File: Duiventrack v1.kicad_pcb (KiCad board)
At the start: 2 copper layers, 22.6 x 12.8 mm, 30 parts, among them P1 CONN_01X07, P2 CONN_01X02, U1 MCP1711-SOT23-5, U2 SP-ABZ-G

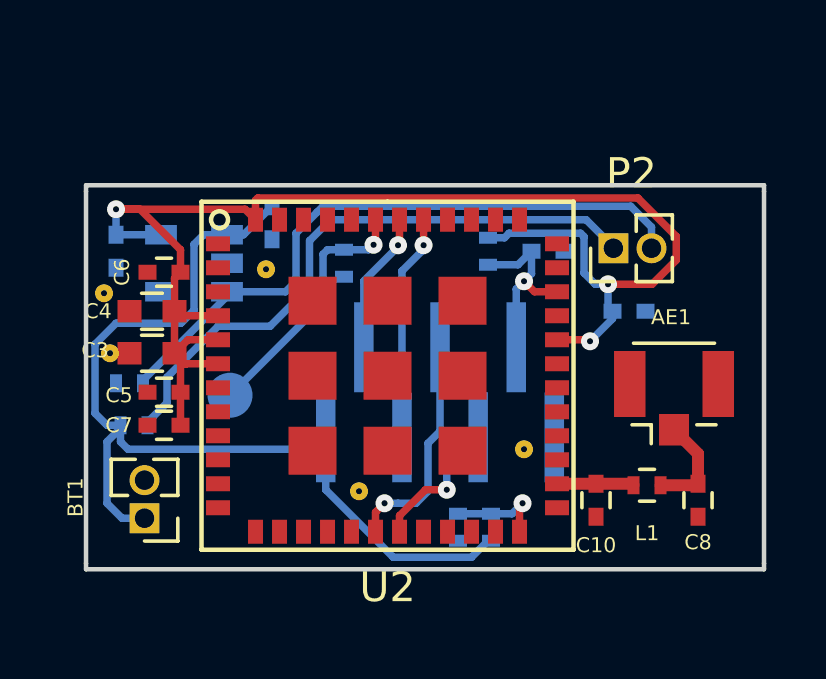
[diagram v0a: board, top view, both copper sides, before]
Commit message: Ground vias toegevoegd
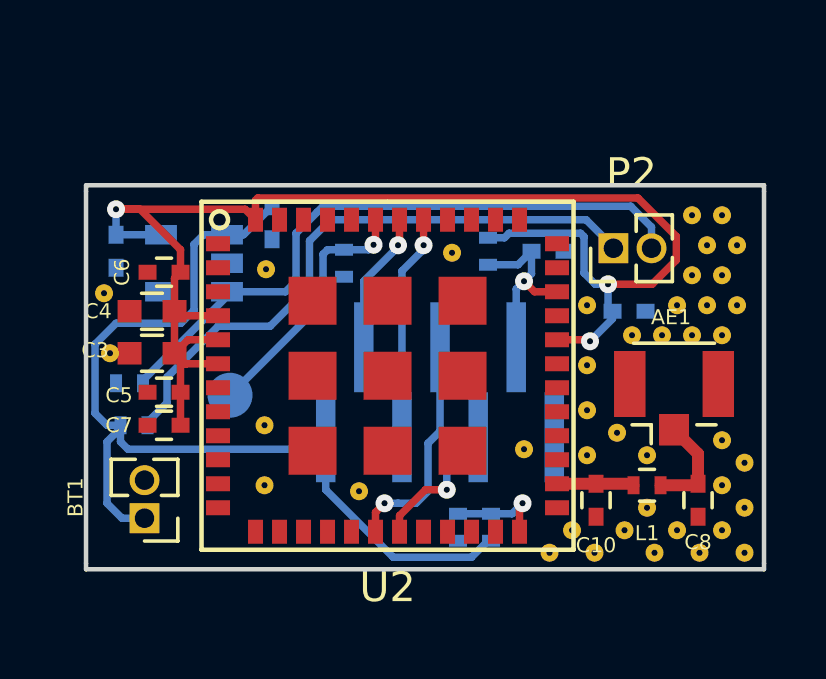
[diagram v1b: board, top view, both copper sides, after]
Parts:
- added REF**: Via 0,6 0,2, Footprint:Via0,6, F.Cu at (145.8, 95.0)
- added REF**: Via 0,6 0,2, Footprint:Via0,6, F.Cu at (158.8, 97.2)
- added REF**: Via 0,6 0,2, Footprint:Via0,6, F.Cu at (158.5, 95.8)
- added REF**: Via 0,6 0,2, Footprint:Via0,6, F.Cu at (159.5, 96.5)
- added REF**: Via 0,6 0,2, Footprint:Via0,6, F.Cu at (160.2, 97.2)
- added REF**: Via 0,6 0,2, Footprint:Via0,6, F.Cu at (161.8, 97.2)
- added REF**: Via 0,6 0,2, Footprint:Via0,6, F.Cu at (161.0, 96.5)
- added REF**: Via 0,6 0,2, Footprint:Via0,6, F.Cu at (161.8, 95.8)
- added REF**: Via 0,6 0,2, Footprint:Via0,6, F.Cu at (161.0, 95.0)
- added REF**: Via 0,6 0,2, Footprint:Via0,6, F.Cu at (156.5, 91.0)
- added REF**: Via 0,6 0,2, Footprint:Via0,6, F.Cu at (156.5, 92.5)
- added REF**: Via 0,6 0,2, Footprint:Via0,6, F.Cu at (145.8, 93.0)
- added REF**: Via 0,6 0,2, Footprint:Via0,6, F.Cu at (161.8, 94.2)
- added REF**: Via 0,6 0,2, Footprint:Via0,6, F.Cu at (160.0, 86.0)
- added REF**: Via 0,6 0,2, Footprint:Via0,6, F.Cu at (161.0, 86.0)
- added REF**: Via 0,6 0,2, Footprint:Via0,6, F.Cu at (161.5, 87.0)
- added REF**: Via 0,6 0,2, Footprint:Via0,6, F.Cu at (160.5, 87.0)
- added REF**: Via 0,6 0,2, Footprint:Via0,6, F.Cu at (160.0, 88.0)
- added REF**: Via 0,6 0,2, Footprint:Via0,6, F.Cu at (161.0, 88.0)
- added REF**: Via 0,6 0,2, Footprint:Via0,6, F.Cu at (161.5, 89.0)
- added REF**: Via 0,6 0,2, Footprint:Via0,6, F.Cu at (160.5, 89.0)
- added REF**: Via 0,6 0,2, Footprint:Via0,6, F.Cu at (159.5, 89.0)
- added REF**: Via 0,6 0,2, Footprint:Via0,6, F.Cu at (152.0, 87.2)
- added REF**: Via 0,6 0,2, Footprint:Via0,6, F.Cu at (161.0, 93.5)
- added REF**: Via 0,6 0,2, Footprint:Via0,6, F.Cu at (157.5, 93.2)
- added REF**: Via 0,6 0,2, Footprint:Via0,6, F.Cu at (156.5, 94.0)
- added REF**: Via 0,6 0,2, Footprint:Via0,6, F.Cu at (161.0, 90.0)
- added REF**: Via 0,6 0,2, Footprint:Via0,6, F.Cu at (160.0, 90.0)
- added REF**: Via 0,6 0,2, Footprint:Via0,6, F.Cu at (159.0, 90.0)
- added REF**: Via 0,6 0,2, Footprint:Via0,6, F.Cu at (156.5, 89.0)
- added REF**: Via 0,6 0,2, Footprint:Via0,6, F.Cu at (158.0, 90.0)
- added REF**: Via 0,6 0,2, Footprint:Via0,6, F.Cu at (158.5, 94.0)
- added REF**: Via 0,6 0,2, Footprint:Via0,6, F.Cu at (155.2, 97.2)
- added REF**: Via 0,6 0,2, Footprint:Via0,6, F.Cu at (156.0, 96.5)
- added REF**: Via 0,6 0,2, Footprint:Via0,6, F.Cu at (156.8, 97.2)
- added REF**: Via 0,6 0,2, Footprint:Via0,6, F.Cu at (157.8, 96.5)

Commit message: Crystal toegevoegd
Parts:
- removed the REF** at (145.8, 95.0)
- removed the REF** at (158.8, 97.2)
- removed the REF** at (158.5, 95.8)
- removed the REF** at (159.5, 96.5)
- removed the REF** at (160.2, 97.2)
- removed the REF** at (161.8, 97.2)
- removed the REF** at (161.0, 96.5)
- removed the REF** at (161.8, 95.8)
- removed the REF** at (161.0, 95.0)
- removed the REF** at (156.5, 92.5)
- removed the REF** at (145.8, 93.0)
- removed the REF** at (161.8, 94.2)
- removed the REF** at (160.0, 86.0)
- removed the REF** at (161.0, 86.0)
- removed the REF** at (161.5, 87.0)
- removed the REF** at (160.5, 87.0)
- removed the REF** at (160.0, 88.0)
- removed the REF** at (161.0, 88.0)
- removed the REF** at (161.5, 89.0)
- removed the REF** at (160.5, 89.0)
- removed the REF** at (159.5, 89.0)
- removed the REF** at (152.0, 87.2)
- removed the REF** at (161.0, 93.5)
- removed the REF** at (157.5, 93.2)
- removed the REF** at (161.0, 90.0)
- removed the REF** at (160.0, 90.0)
- removed the REF** at (159.0, 90.0)
- removed the REF** at (148.9, 95.2)
- removed the REF** at (145.8, 87.8)
- removed the REF** at (140.6, 90.6)
- removed the REF** at (154.4, 93.8)
- removed the REF** at (156.5, 89.0)
- removed the REF** at (140.4, 88.6)
- removed the REF** at (158.0, 90.0)
- removed the REF** at (158.5, 94.0)
- removed the REF** at (155.2, 97.2)
- removed the REF** at (156.0, 96.5)
- removed the REF** at (156.8, 97.2)
- removed the REF** at (157.8, 96.5)
- added C12: 20pF, Capacitors_SMD:C_0402, F.Cu at (151.5, 83.9)
- added C13: 20pF, Capacitors_SMD:C_0402, F.Cu at (143.5, 83.9)
- added REF**: Via 0,6 0,2, Footprint:Via0,6, F.Cu at (159.5, 86.0)
- added REF**: Via 0,6 0,2, Footprint:Via0,6, F.Cu at (157.5, 93.5)
- added REF**: Via 0,6 0,2, Footprint:Via0,6, F.Cu at (156.5, 93.0)
- added REF**: Via 0,6 0,2, Footprint:Via0,6, F.Cu at (156.5, 92.0)
- added REF**: Via 0,6 0,2, Footprint:Via0,6, F.Cu at (155.5, 97.0)
- added REF**: Via 0,6 0,2, Footprint:Via0,6, F.Cu at (156.5, 97.0)
- added REF**: Via 0,6 0,2, Footprint:Via0,6, F.Cu at (157.5, 97.0)
- added REF**: Via 0,6 0,2, Footprint:Via0,6, F.Cu at (158.0, 96.0)
- added REF**: Via 0,6 0,2, Footprint:Via0,6, F.Cu at (158.5, 97.0)
- added REF**: Via 0,6 0,2, Footprint:Via0,6, F.Cu at (145.9, 92.8)
- added REF**: Via 0,6 0,2, Footprint:Via0,6, F.Cu at (159.0, 96.0)
- added REF**: Via 0,6 0,2, Footprint:Via0,6, F.Cu at (159.5, 97.0)
- added REF**: Via 0,6 0,2, Footprint:Via0,6, F.Cu at (160.5, 97.0)
- added REF**: Via 0,6 0,2, Footprint:Via0,6, F.Cu at (161.5, 96.5)
- added REF**: Via 0,6 0,2, Footprint:Via0,6, F.Cu at (161.5, 95.5)
- added REF**: Via 0,6 0,2, Footprint:Via0,6, F.Cu at (161.0, 94.5)
- added REF**: Via 0,6 0,2, Footprint:Via0,6, F.Cu at (161.5, 93.5)
- added REF**: Via 0,6 0,2, Footprint:Via0,6, F.Cu at (160.5, 88.0)
- added REF**: Via 0,6 0,2, Footprint:Via0,6, F.Cu at (161.5, 88.0)
- added REF**: Via 0,6 0,2, Footprint:Via0,6, F.Cu at (161.0, 89.0)
- added REF**: Via 0,6 0,2, Footprint:Via0,6, F.Cu at (143.2, 97.1)
- added REF**: Via 0,6 0,2, Footprint:Via0,6, F.Cu at (160.0, 89.0)
- added REF**: Via 0,6 0,2, Footprint:Via0,6, F.Cu at (158.5, 90.0)
- added REF**: Via 0,6 0,2, Footprint:Via0,6, F.Cu at (159.5, 90.0)
- added REF**: Via 0,6 0,2, Footprint:Via0,6, F.Cu at (160.5, 90.0)
- added REF**: Via 0,6 0,2, Footprint:Via0,6, F.Cu at (161.5, 90.0)
- added REF**: Via 0,6 0,2, Footprint:Via0,6, F.Cu at (154.2, 93.7)
- added REF**: Via 0,6 0,2, Footprint:Via0,6, F.Cu at (140.8, 90.6)
- added REF**: Via 0,6 0,2, Footprint:Via0,6, F.Cu at (145.8, 87.9)
- added REF**: Via 0,6 0,2, Footprint:Via0,6, F.Cu at (148.8, 95.2)
- added REF**: Via 0,6 0,2, Footprint:Via0,6, F.Cu at (145.5, 95.2)
- added REF**: Via 0,6 0,2, Footprint:Via0,6, F.Cu at (160.0, 87.0)
- added REF**: Via 0,6 0,2, Footprint:Via0,6, F.Cu at (159.0, 88.5)
- added REF**: Via 0,6 0,2, Footprint:Via0,6, F.Cu at (160.5, 86.0)
- added REF**: Via 0,6 0,2, Footprint:Via0,6, F.Cu at (161.0, 87.0)
- added REF**: Via 0,6 0,2, Footprint:Via0,6, F.Cu at (161.5, 86.0)
- added Y1: Crystal, Crystals:Crystal_SMD_5032-2pin_5.0x3.2mm, F.Cu at (147.5, 83.2)
- moved C1 0.27 mm to (145.9, 86.5)
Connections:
- U2 pad 1: (no net) -> PA12
- U2 pad 45: (no net) -> Net-(C12-Pad1)
- U2 pad 46: (no net) -> Net-(C13-Pad1)
- U2 pad 48: +3V3 -> PA12
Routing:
- net Net-(C12-Pad1): track 0.00 -> 6.05 mm
- net Net-(C13-Pad1): track 0.00 -> 5.95 mm
- net +3V3: track 48.9 -> 43.2 mm, vias 3 -> 4
- net PA12: track 0.00 -> 1.58 mm
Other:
- board size 22.6 x 12.8 mm -> 22.6 x 16.9 mm

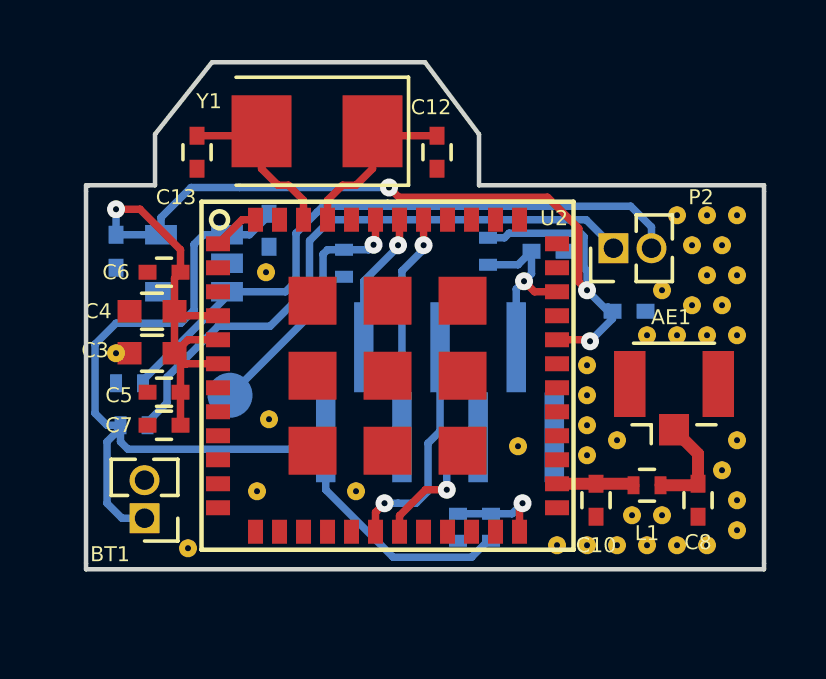
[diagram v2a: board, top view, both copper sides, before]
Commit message: Revert "Crystal toegevoegd"
This reverts commit 51f246dfdab6a70a9bd41b0f28c72966c573f5f4.
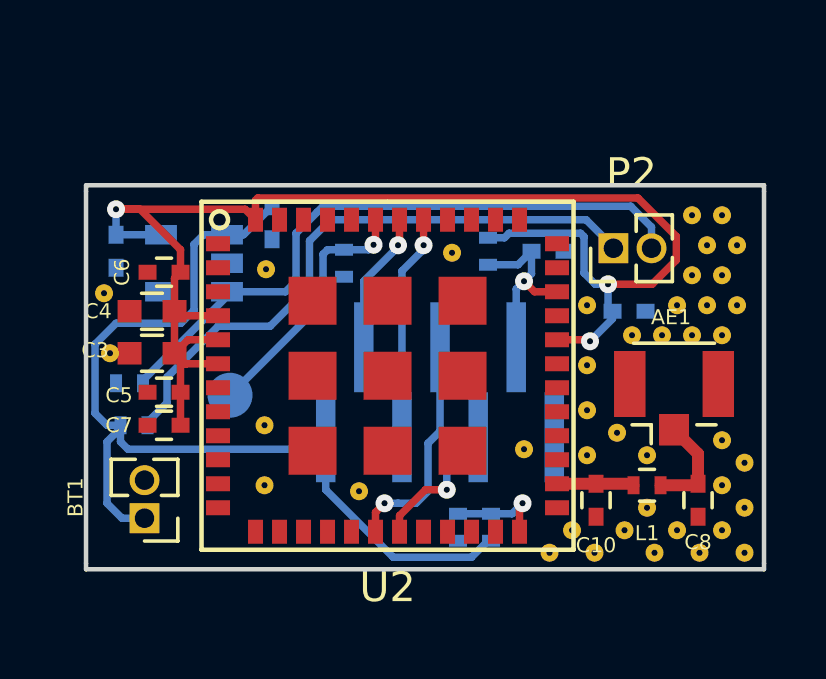
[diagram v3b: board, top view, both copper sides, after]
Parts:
- removed C12, C13: 20pF, Capacitors_SMD:C_0402
- removed the REF** at (159.5, 86.0)
- removed the REF** at (157.5, 93.5)
- removed the REF** at (156.5, 93.0)
- removed the REF** at (156.5, 92.0)
- removed the REF** at (155.5, 97.0)
- removed the REF** at (156.5, 97.0)
- removed the REF** at (157.5, 97.0)
- removed the REF** at (158.0, 96.0)
- removed the REF** at (158.5, 97.0)
- removed the REF** at (145.9, 92.8)
- removed the REF** at (159.0, 96.0)
- removed the REF** at (159.5, 97.0)
- removed the REF** at (160.5, 97.0)
- removed the REF** at (161.5, 96.5)
- removed the REF** at (161.5, 95.5)
- removed the REF** at (161.0, 94.5)
- removed the REF** at (161.5, 93.5)
- removed the REF** at (160.5, 88.0)
- removed the REF** at (161.5, 88.0)
- removed the REF** at (161.0, 89.0)
- removed the REF** at (143.2, 97.1)
- removed the REF** at (160.0, 89.0)
- removed the REF** at (158.5, 90.0)
- removed the REF** at (159.5, 90.0)
- removed the REF** at (160.5, 90.0)
- removed the REF** at (161.5, 90.0)
- removed the REF** at (154.2, 93.7)
- removed the REF** at (140.8, 90.6)
- removed the REF** at (145.8, 87.9)
- removed the REF** at (148.8, 95.2)
- removed the REF** at (145.5, 95.2)
- removed the REF** at (160.0, 87.0)
- removed the REF** at (159.0, 88.5)
- removed the REF** at (160.5, 86.0)
- removed the REF** at (161.0, 87.0)
- removed the REF** at (161.5, 86.0)
- removed Y1: Crystal, Crystals:Crystal_SMD_5032-2pin_5.0x3.2mm
- added REF**: Via 0,6 0,2, Footprint:Via0,6, F.Cu at (145.8, 95.0)
- added REF**: Via 0,6 0,2, Footprint:Via0,6, F.Cu at (158.8, 97.2)
- added REF**: Via 0,6 0,2, Footprint:Via0,6, F.Cu at (158.5, 95.8)
- added REF**: Via 0,6 0,2, Footprint:Via0,6, F.Cu at (159.5, 96.5)
- added REF**: Via 0,6 0,2, Footprint:Via0,6, F.Cu at (160.2, 97.2)
- added REF**: Via 0,6 0,2, Footprint:Via0,6, F.Cu at (161.8, 97.2)
- added REF**: Via 0,6 0,2, Footprint:Via0,6, F.Cu at (161.0, 96.5)
- added REF**: Via 0,6 0,2, Footprint:Via0,6, F.Cu at (161.8, 95.8)
- added REF**: Via 0,6 0,2, Footprint:Via0,6, F.Cu at (161.0, 95.0)
- added REF**: Via 0,6 0,2, Footprint:Via0,6, F.Cu at (156.5, 92.5)
- added REF**: Via 0,6 0,2, Footprint:Via0,6, F.Cu at (145.8, 93.0)
- added REF**: Via 0,6 0,2, Footprint:Via0,6, F.Cu at (161.8, 94.2)
- added REF**: Via 0,6 0,2, Footprint:Via0,6, F.Cu at (160.0, 86.0)
- added REF**: Via 0,6 0,2, Footprint:Via0,6, F.Cu at (161.0, 86.0)
- added REF**: Via 0,6 0,2, Footprint:Via0,6, F.Cu at (161.5, 87.0)
- added REF**: Via 0,6 0,2, Footprint:Via0,6, F.Cu at (160.5, 87.0)
- added REF**: Via 0,6 0,2, Footprint:Via0,6, F.Cu at (160.0, 88.0)
- added REF**: Via 0,6 0,2, Footprint:Via0,6, F.Cu at (161.0, 88.0)
- added REF**: Via 0,6 0,2, Footprint:Via0,6, F.Cu at (161.5, 89.0)
- added REF**: Via 0,6 0,2, Footprint:Via0,6, F.Cu at (160.5, 89.0)
- added REF**: Via 0,6 0,2, Footprint:Via0,6, F.Cu at (159.5, 89.0)
- added REF**: Via 0,6 0,2, Footprint:Via0,6, F.Cu at (152.0, 87.2)
- added REF**: Via 0,6 0,2, Footprint:Via0,6, F.Cu at (161.0, 93.5)
- added REF**: Via 0,6 0,2, Footprint:Via0,6, F.Cu at (157.5, 93.2)
- added REF**: Via 0,6 0,2, Footprint:Via0,6, F.Cu at (161.0, 90.0)
- added REF**: Via 0,6 0,2, Footprint:Via0,6, F.Cu at (160.0, 90.0)
- added REF**: Via 0,6 0,2, Footprint:Via0,6, F.Cu at (159.0, 90.0)
- added REF**: Via 0,6 0,2, Footprint:Via0,6, F.Cu at (148.9, 95.2)
- added REF**: Via 0,6 0,2, Footprint:Via0,6, F.Cu at (145.8, 87.8)
- added REF**: Via 0,6 0,2, Footprint:Via0,6, F.Cu at (140.6, 90.6)
- added REF**: Via 0,6 0,2, Footprint:Via0,6, F.Cu at (154.4, 93.8)
- added REF**: Via 0,6 0,2, Footprint:Via0,6, F.Cu at (156.5, 89.0)
- added REF**: Via 0,6 0,2, Footprint:Via0,6, F.Cu at (140.4, 88.6)
- added REF**: Via 0,6 0,2, Footprint:Via0,6, F.Cu at (158.0, 90.0)
- added REF**: Via 0,6 0,2, Footprint:Via0,6, F.Cu at (158.5, 94.0)
- added REF**: Via 0,6 0,2, Footprint:Via0,6, F.Cu at (155.2, 97.2)
- added REF**: Via 0,6 0,2, Footprint:Via0,6, F.Cu at (156.0, 96.5)
- added REF**: Via 0,6 0,2, Footprint:Via0,6, F.Cu at (156.8, 97.2)
- added REF**: Via 0,6 0,2, Footprint:Via0,6, F.Cu at (157.8, 96.5)
- moved C1 0.27 mm to (146.0, 86.2)
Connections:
- U2 pad 1: PA12 -> (no net)
- U2 pad 45: Net-(C12-Pad1) -> (no net)
- U2 pad 46: Net-(C13-Pad1) -> (no net)
- U2 pad 48: PA12 -> +3V3
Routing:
- net Net-(C12-Pad1): track 6.05 -> 0.00 mm
- net Net-(C13-Pad1): track 5.95 -> 0.00 mm
- net +3V3: track 43.2 -> 48.9 mm, vias 4 -> 3
- net PA12: track 1.58 -> 0.00 mm
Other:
- board size 22.6 x 16.9 mm -> 22.6 x 12.8 mm

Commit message: drie solderjumpers toegevoegd, nog aan te sluiten
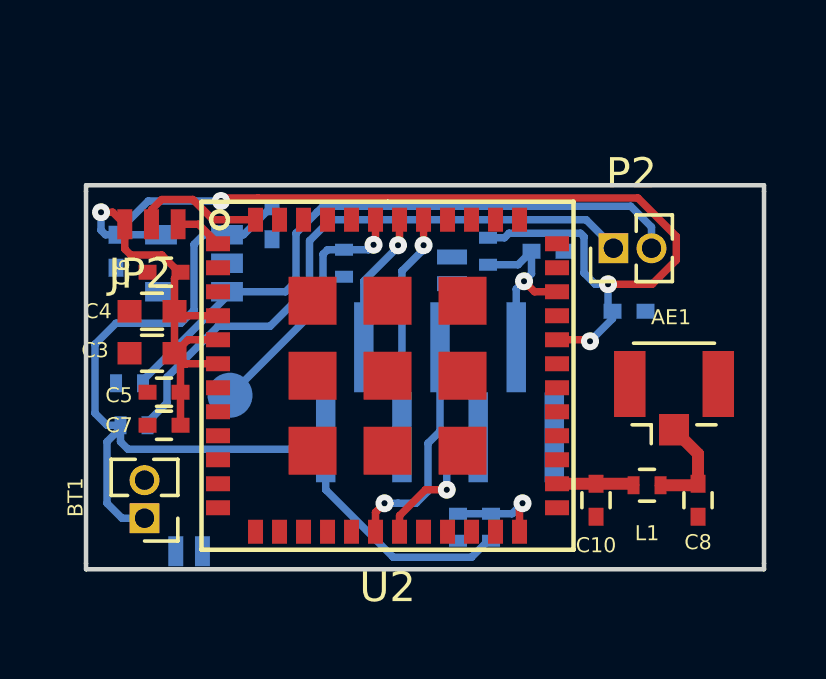
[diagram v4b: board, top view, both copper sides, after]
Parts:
- removed REF** (x41): Via 0,6 0,2, Footprint:Via0,6
- added JP1: Jumper_NO_Small, Footprint:SolderJumper_NO, B.Cu at (152.0, 87.9)
- added JP2: Jumper_NC_Dual, Footprint:SolderJumper_NO-3, F.Cu at (141.6, 86.3)
- added JP3: Jumper_NO_Small, Footprint:SolderJumper_NO, B.Cu at (143.3, 97.2)
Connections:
- U2 pad 1: (no net) -> Net-(JP2-Pad3)
- U2 pad 10: (no net) -> Net-(JP3-Pad1)
- U2 pad 21: (no net) -> Net-(JP3-Pad2)
- U2 pad 46: (no net) -> Net-(JP1-Pad2)
- U2 pad 47: (no net) -> Net-(JP1-Pad1)
- U2 pad 48: +3V3 -> Net-(JP2-Pad2)
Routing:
- net Net-(JP2-Pad2): track 0.00 -> 4.37 mm
- net Net-(JP2-Pad3): track 0.00 -> 1.60 mm
- net +3V3: track 48.9 -> 49.4 mm, vias 3 -> 4
